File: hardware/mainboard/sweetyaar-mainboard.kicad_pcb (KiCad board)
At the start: 4 copper layers, 80 x 80 mm, 104 parts, among them Q1 MMBT3904

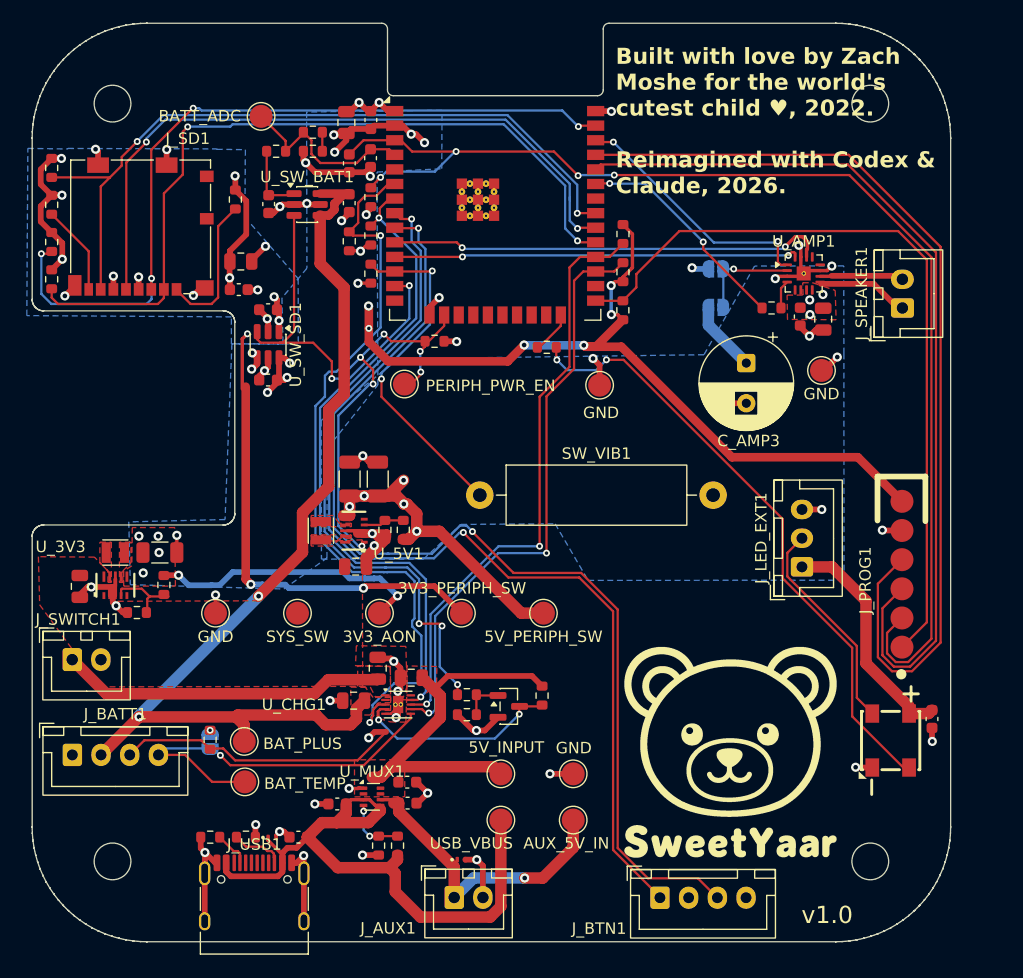
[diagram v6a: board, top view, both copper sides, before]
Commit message: Adding large silkscreen text next to connectors
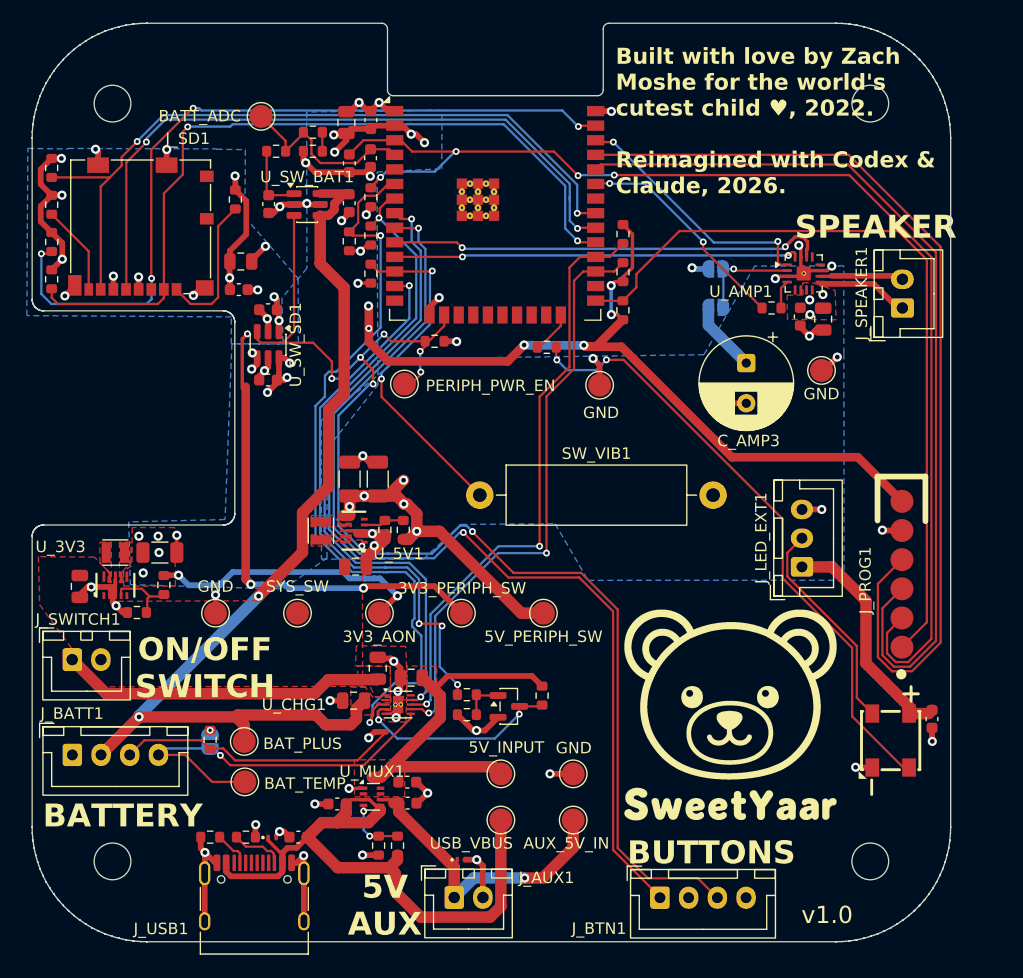
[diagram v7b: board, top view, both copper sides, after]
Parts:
- moved LOGO 3.25 mm to (80.8, 80.2)
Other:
- board text added: "5V AUX"
- board text added: "BATTERY"
- board text added: "BUTTONS"
- board text added: "ON/OFF SWITCH"
- board text added: "SPEAKER"
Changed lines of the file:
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@@
 		(tags "usb usb-c 2.0 pd")
 		(property "Reference" "J_USB1"
-			(at 0 -5.645 0)
+			(at -8.125 1.705 0)
 			(layer "F.SilkS")
 			(effects
@@
 		(tags "connector JST XH vertical")
 		(property "Reference" "J_BATT1"
-			(at 3.75 -3.55 0)
+			(at -0.025 -3.6 0)
 			(layer "F.SilkS")
 			(effects
@@
 		)
 		(property "Value" "SYS_SW"
-			(at 0 2.05 0)
+			(at 0 -2.325 0)
 			(layer "F.SilkS")
 			(effects
@@
 		)
 		(property "Value" "GND"
-			(at 0 2.05 0)
+			(at 0 -2.325 0)
 			(layer "F.SilkS")
 			(effects
@@
 		(tags "TQFN NoLead")
 		(property "Reference" "U_AMP1"
-			(at 0 -2.8 0)
+			(at -5.475 1.5825 0)
 			(layer "F.SilkS")
 			(effects
@@
 		(tags "connector JST XH vertical")
 		(property "Reference" "J_AUX1"
-			(at -5.76 2.68 0)
+			(at 8.04 -1.72 0)
 			(layer "F.SilkS")
 			(effects
@@
 	(footprint "SweetYaar:Logo_SweetYaar_Teddy_20x20mm"
 		(layer "F.Cu")
-		(at 80.825 83.5)
+		(at 80.825 80.25)
 		(descr "Teddy face and SweetYaar wordmark; 20 x 20 mm placement area; front silkscreen only; flip for rear.")
 		(tags "logo teddy bear SweetYaar silkscreen")
@@
 		)
 	)
+	(gr_text "BATTERY"
+		(at 20.925 90.2 0)
+		(layer "F.SilkS")
+		(effects
+			(font
+				(size 2 2)
+				(thickness 0.4)
+				(bold yes)
+			)
+			(justify left bottom)
+		)
+	)
+	(gr_text "BUTTONS"
+		(at 71.83 93.415 0)
+		(layer "F.SilkS")
+		(effects
+			(font
+				(size 2 2)
+				(thickness 0.4)
+				(bold yes)
+			)
+			(justify left bottom)
+		)
+	)
+	(gr_text "SPEAKER"
+		(at 86.425 38.925 0)
+		(layer "F.SilkS")
+		(effects
+			(font
+				(size 2 2)
+				(thickness 0.4)
+				(bold yes)
+			)
+			(justify left bottom)
+		)
+	)
+	(gr_text "ON/OFF\nSWITCH"
+		(at 35.05 78.935 0)
+		(layer "F.SilkS")
+		(effects
+			(font
+				(size 2 2)
+				(thickness 0.4)
+				(bold yes)
+			)
+			(justify bottom)
+		)
+	)
+	(gr_text "5V\nAUX"
+		(at 50.725 99.625 0)
+		(layer "F.SilkS")
+		(effects
+			(font
+				(size 2 2)
+				(thickness 0.4)
+				(bold yes)
+			)
+			(justify bottom)
+		)
+	)

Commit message: Changing CHARGING_ENABLE to GPIO4
previous GPIO was held down momentarily on reset by the ESP and this could potentially allow charging without finishing setting up battery profile.
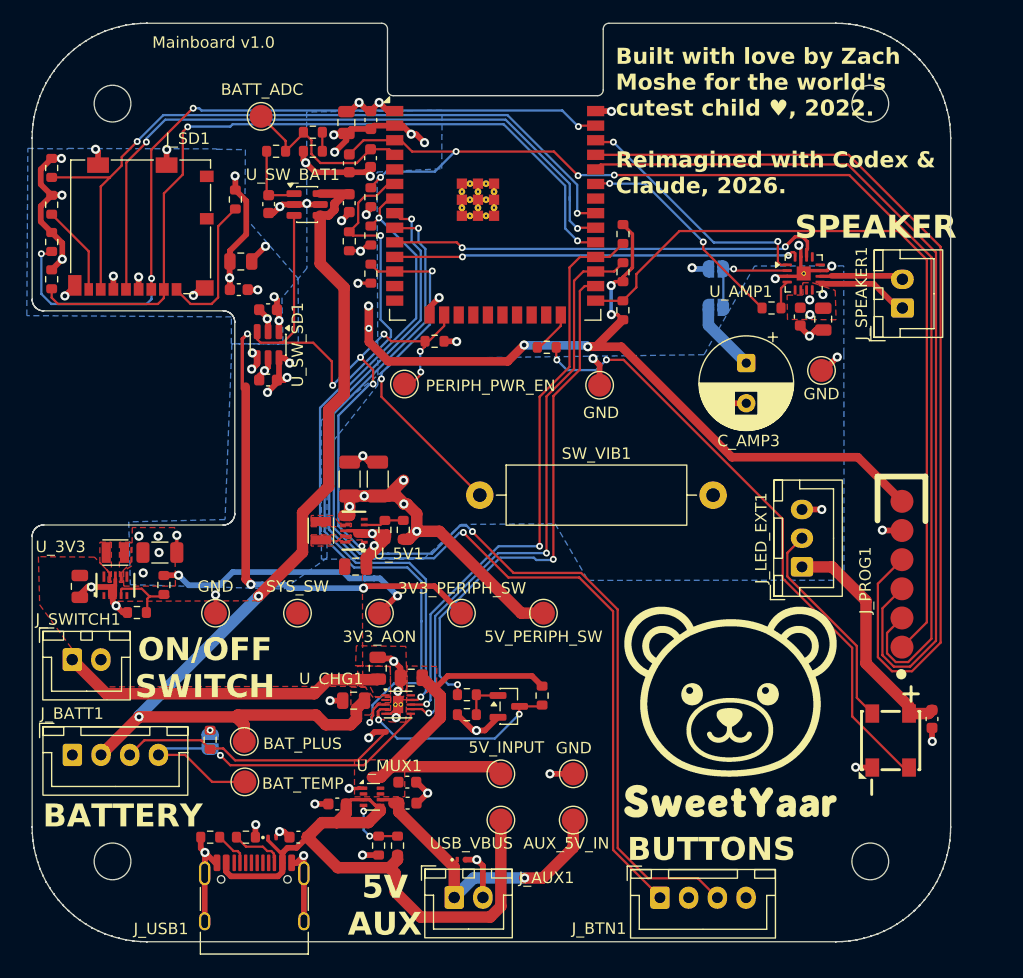
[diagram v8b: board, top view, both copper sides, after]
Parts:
- moved LOGO 0.25 mm to (80.8, 80.0)
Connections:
- U_ESP32 pad 13: /CHARGER_ENABLE -> unconnected-(U_ESP32-IO14-Pad13)
- U_ESP32 pad 26: unconnected-(U_ESP32-IO4-Pad26) -> /CHARGER_ENABLE
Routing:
- net /CHARGER_ENABLE: track 48.9 -> 45.8 mm, vias 4 -> 2
- net /PERIPH_PWR_EN: track 59.1 -> 59.9 mm
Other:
- board text added: "IMPORTANT: NEVER CLOSE BOTH!"
- board text added: "If both jumpers are open, volume is at a default level (9 dB). Close one of the jumpers to change settings."
- board text added: "Mainboard v1.0"
- board text removed: "If both jumpers are open, volume is at a default level (9 dB). Close one of the jumpers to change settings. IMPORTANT: NEVER CLOSE BOTH!"
- board text removed: "v1.0"
